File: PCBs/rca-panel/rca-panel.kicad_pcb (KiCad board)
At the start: 2 copper layers, 141 x 52.1 mm, 27 parts

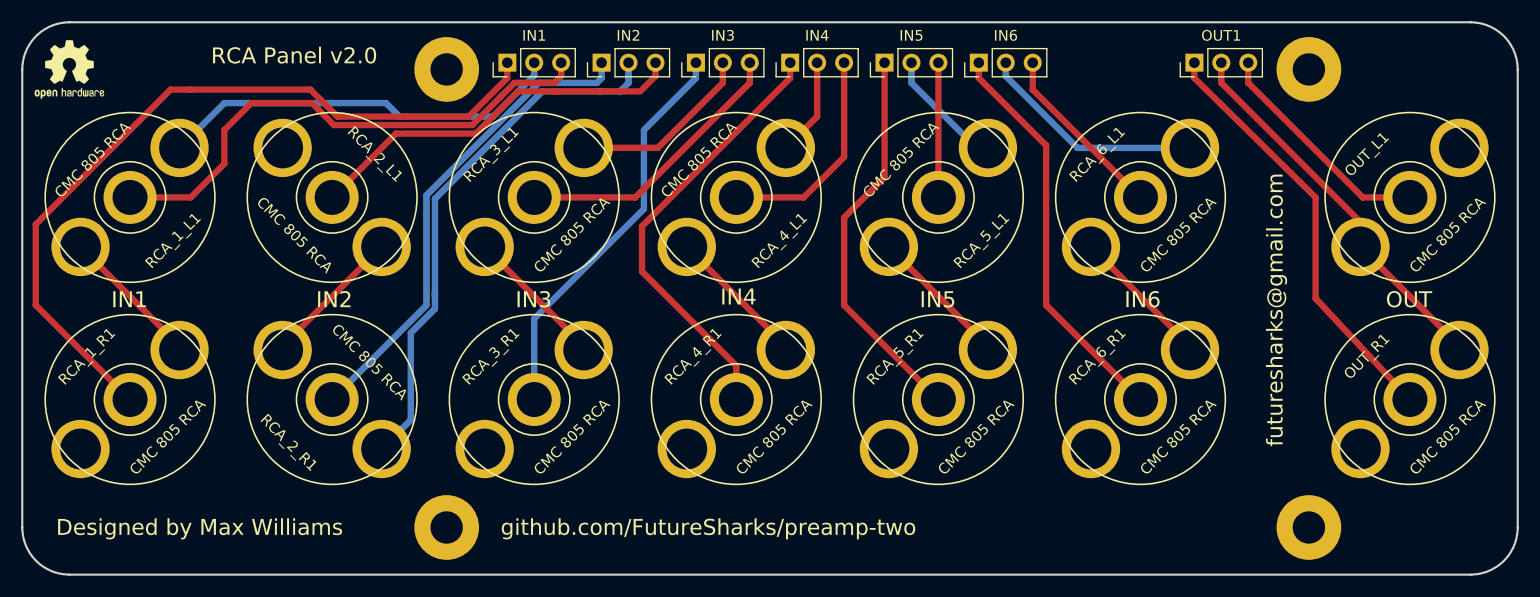
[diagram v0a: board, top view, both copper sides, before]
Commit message: updating PCB after creating new library for newer 805 RCAs
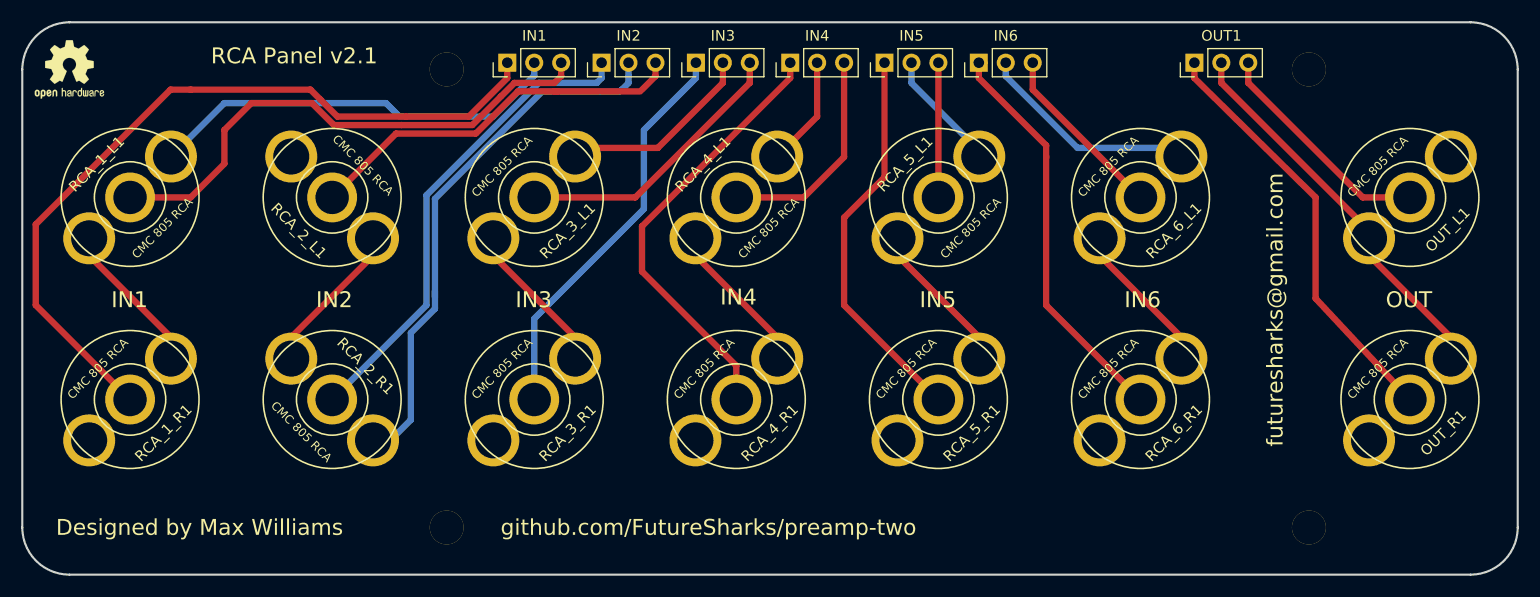
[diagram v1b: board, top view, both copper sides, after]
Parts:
- OUT_L1, OUT_R1, RCA_1_L1, RCA_1_R1, RCA_2_L1, RCA_2_R1, RCA_3_L1, RCA_3_R1, RCA_4_L1, RCA_4_R1, RCA_5_L1, RCA_5_R1, RCA_6_L1, RCA_6_R1: footprint rca-panel:cmc-805 -> rca-panel:cmc-805-new
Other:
- board text added: "RCA Panel v2.1"
- board text removed: "RCA Panel v2.0"
